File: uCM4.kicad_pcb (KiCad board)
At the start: 2 copper layers, 55 x 48 mm, 77 parts, among them IC1 MAX17048G+, J10 USB_C_Receptacle, J12 Conn_02x08_Odd_Even, J13 Conn_02x07_Odd_Even, J2 Micro_SD_Card_Det, J4 Conn_01x04, J5 DummyJ, J6 DummyJ, J8 Camera 0, J9 Camera 1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

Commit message: Routing
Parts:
- removed TP1, TP3, TP4, TP5, TP6, TP7, TP9: TestPoint, TestPoint:TestPoint_Pad_D1.0mm
- removed U3: TPD4EUSB30DQAR, Package_SON:USON-10_2.5x1.0mm_P0.5mm
- added U5: TPD2EUSB30, Package_TO_SOT_SMD:Texas_DRT-3, F.Cu at (150.0, 125.8)
- moved TP10 34.3 mm to (122.5, 125.0)
- moved TP11 32.6 mm to (122.5, 129.2)
- moved TP2 9.05 mm to (142.8, 105.2)
- moved TP8 8.63 mm to (133.8, 96.5)
- moved TP12 8.49 mm to (140.0, 107.8)
- moved S2 0.75 mm to (158.5, 108.8)
- moved S1 0.25 mm to (158.5, 99.5)
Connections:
- Module1 pad 37: /ENV_SEL -> unconnected-(Module1A-GPIO7-Pad37)
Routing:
- net GND: track 1.88 -> 137.5 mm, vias 29 -> 95
- net +3V3: track 14.8 -> 141.7 mm, vias 0 -> 19
- net /CAM_GPIO: track 0.00 -> 77.1 mm, vias 0 -> 9
- net /USB_P: track 11.8 -> 78.7 mm, vias 0 -> 1
- net /USB_N: track 13.0 -> 78.2 mm, vias 0 -> 1
- net +5V: track 32.8 -> 97.9 mm, vias 2 -> 8
- net /SCL0: track 40.2 -> 102.7 mm, vias 4 -> 5
- net /RESET: track 0.00 -> 62.0 mm, vias 0 -> 3
- net /SDA0: track 45.2 -> 107.0 mm, vias 4 -> 6
- net Net-(Module1A-Global_EN): track 3.85 -> 59.3 mm, vias 0 -> 3
- net /TXD0: track 0.00 -> 50.3 mm, vias 0 -> 5
- net Net-(Module1A-nRPIBOOT): track 0.00 -> 46.5 mm, vias 0 -> 5
- net /SPI6_CE1_N: track 0.00 -> 41.0 mm, vias 0 -> 5
- net /SCL1: track 3.60 -> 42.4 mm, vias 0 -> 5
- net /SPI6_CE0_N: track 0.00 -> 37.6 mm, vias 0 -> 3
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- added copper zone on F.Cu, net GND
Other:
- board text removed: "ACT"
- board text removed: "PWR"
- board text removed: "RESET"
- board text removed: "RPIBOOT"
- board text removed: "RX GND TX"
- board text removed: "USB OTG"

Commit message: Updating LCSC numbers.
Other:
- board text removed: "(C) Kamil Lorenc 2021"
- board text removed: "µCM4-Net v0.2.0"
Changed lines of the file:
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@@
 		(layer "User.2")
-	)
-	(gr_text "µCM4-Net v0.2.0"
-		(at 126.5 111.5 270)
-		(layer "B.SilkS")
-		(effects
-			(font
-				(size 1 1)
-				(thickness 0.15)
-			)
-			(justify mirror)
-		)
-	)
-	(gr_text "(C) Kamil Lorenc 2021"
-		(at 124.5 109.5 270)
-		(layer "B.SilkS")
-		(effects
-			(font
-				(size 1 1)
-				(thickness 0.15)
-			)
-			(justify mirror)
-		)
 	)
 	(gr_text "Check GPS orientation. And pinout needs to change."

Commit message: Minor changes
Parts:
- J2: footprint CM4:SDCARD_MOLEX_503398-1892 -> Connector_Card:microSD_HC_Hirose_DM3AT-SF-PEJM5

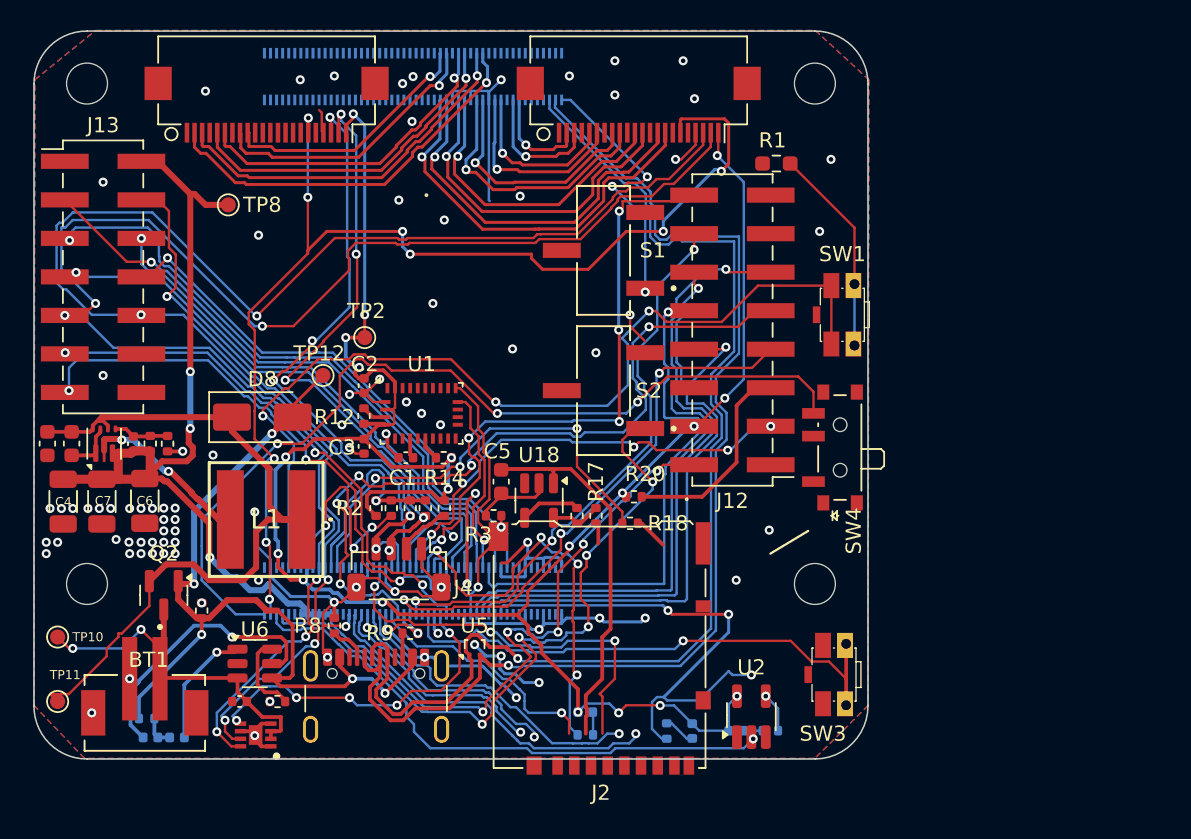
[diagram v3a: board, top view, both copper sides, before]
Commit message: Tuning differential traces and changing some footprints
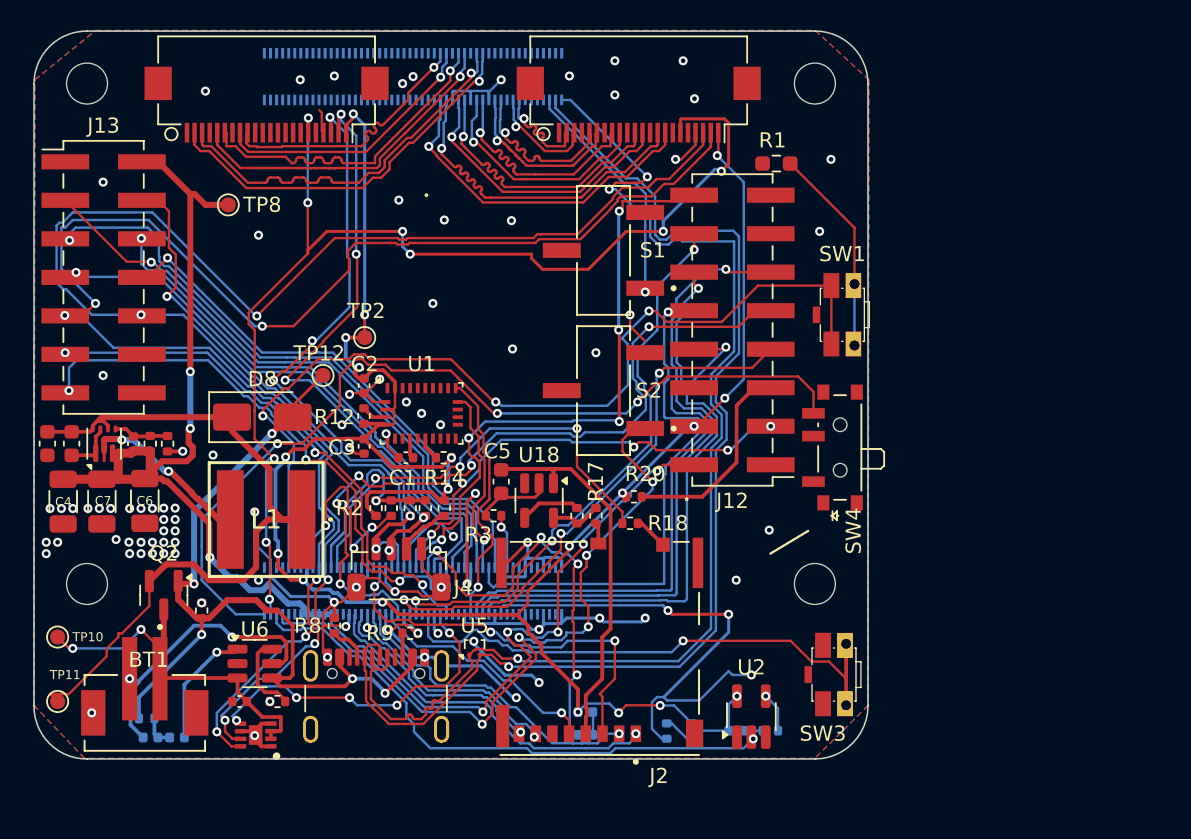
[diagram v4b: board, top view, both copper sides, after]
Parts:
- J2: footprint Connector_Card:microSD_HC_Hirose_DM3AT-SF-PEJM5 -> CM4:SDCARD_MOLEX_503398-1892
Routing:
- net GND: track 137.5 -> 130.3 mm, vias 95 -> 93
- net /CAM1_D3_P: track 26.6 -> 22.9 mm
- net /CAM1_D2_P: track 22.5 -> 19.0 mm
- net /CAM1_C_P: track 17.7 -> 15.4 mm
- net /CAM1_D3_N: track 24.9 -> 22.9 mm
- net /CAM1_D1_P: track 12.8 -> 11.4 mm
- net /CAM1_D2_N: track 20.3 -> 18.9 mm
- net /CAM1_D0_P: track 8.59 -> 7.29 mm
- net /CAM0_D0_P: track 24.5 -> 25.8 mm
- net /CAM0_C_P: track 17.1 -> 18.0 mm
- net /CAM0_C_N: track 18.7 -> 18.0 mm
- net /CAM0_D1_P: track 21.3 -> 22.0 mm
- net /CAM0_D1_N: track 22.6 -> 22.0 mm
- net /USB_P: track 78.7 -> 78.1 mm
- net /SD_CLK: track 16.3 -> 15.7 mm
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
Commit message: Prepping for production.
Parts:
- C5: value 10u -> 10uF
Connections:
- U6 pad 2: unconnected-(U6-GND-Pad2) -> GND
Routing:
- net GND: track 130.3 -> 131.7 mm, vias 93 -> 94
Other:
- board text added: "Shepherd's Eye V1.0 William Nacci Kemere/RNEL + Robinson Labs '25"

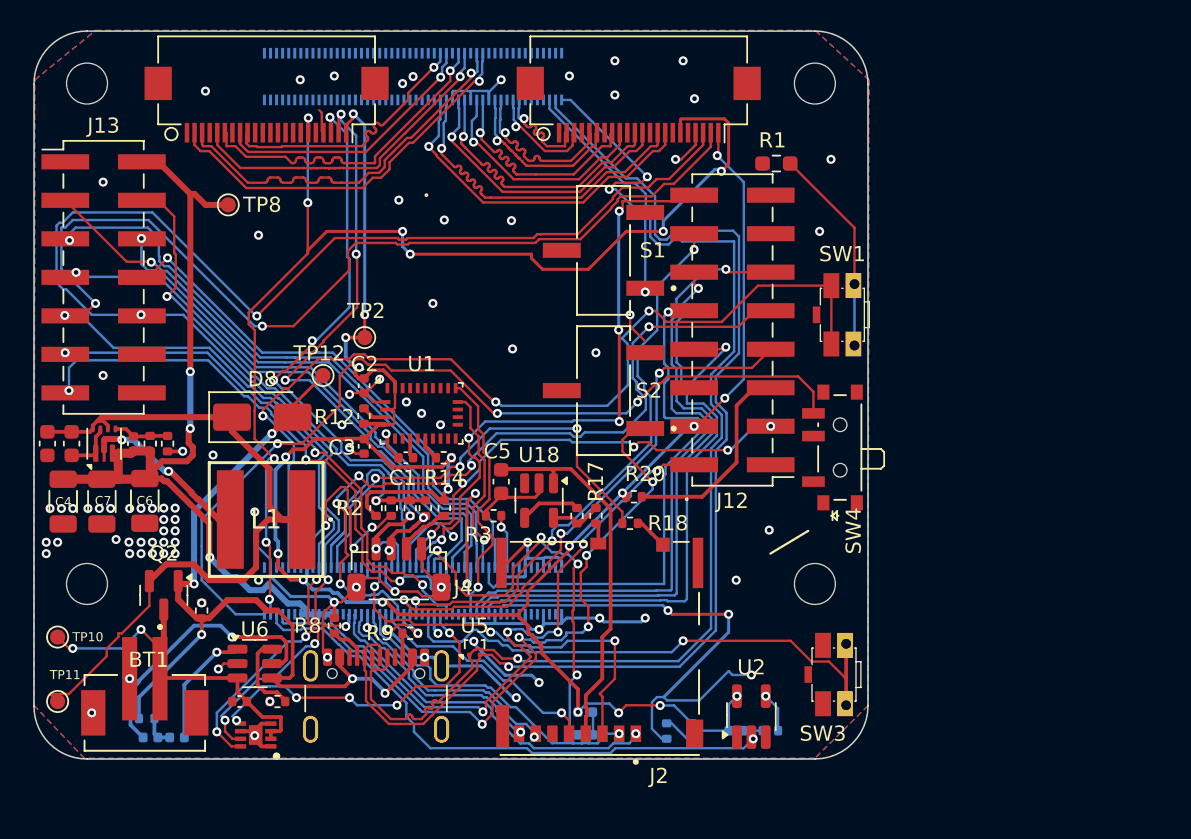
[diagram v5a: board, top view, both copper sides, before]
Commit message: Added new camera connectors. (Had to flip the symbol to match up hirose connection order)
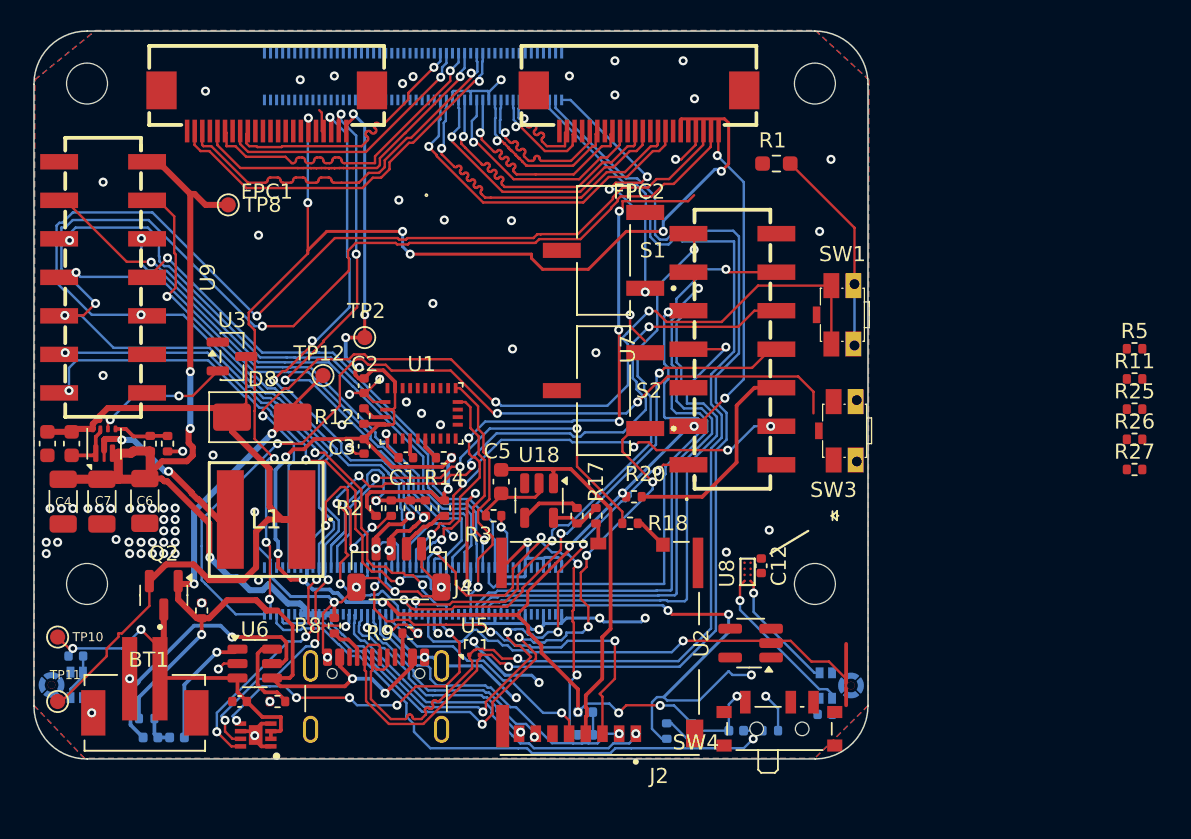
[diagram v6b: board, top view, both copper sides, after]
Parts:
- removed J12: Conn_02x08_Odd_Even, Connector_PinHeader_2.54mm:PinHeader_2x08_P2.54mm_Vertical_SMD
- removed J13: Conn_02x07_Odd_Even, Connector_PinHeader_2.54mm:PinHeader_2x07_P2.54mm_Vertical_SMD
- removed J8: Camera 0, CM4:Hirose_FH12-22S-0.5SH_1x22-1MP_P0.50mm_Horizontal
- removed J9: Camera 1, CM4:Hirose_FH12-22S-0.5SH_1x22-1MP_P0.50mm_Horizontal
- added C10: 100nF, Capacitor_SMD:C_0402_1005Metric, B.Cu at (173.1, 130.1)
- added C12: 100nF, Capacitor_SMD:C_0402_1005Metric, F.Cu at (168.9, 120.3)
- added FPC1: FPC-05F-22PH20, EasyEDA:FPC-SMD_22P-P0.50_FPC-05F-22PH20, F.Cu at (136.3, 90.3)
- added FPC2: FPC-05F-22PH20, EasyEDA:FPC-SMD_22P-P0.50_FPC-05F-22PH20, F.Cu at (160.8, 90.3)
- added MIC1: MMICT390200012, EasyEDA:MIC-SMD_5P-L3.5-W2.7-TL_MMICT390200012, B.Cu at (174.1, 128.2)
- added MIC2: MMICT390200012, EasyEDA:MIC-SMD_5P-L3.5-W2.7-TL_MMICT390200012, B.Cu at (122.8, 128.2)
- added R11: 2.2K 1%, Resistor_SMD:R_0402_1005Metric, F.Cu at (193.5, 108.0)
- added R25: 2.2K 1%, Resistor_SMD:R_0402_1005Metric, F.Cu at (193.5, 110.0)
- added R26: 2.2K 1%, Resistor_SMD:R_0402_1005Metric, F.Cu at (193.5, 112.0)
- added R27: 1k, Resistor_SMD:R_0402_1005Metric, F.Cu at (193.5, 114.0)
- added R5: 2.2K 1%, Resistor_SMD:R_0402_1005Metric, F.Cu at (193.5, 106.0)
- added U3: TPS3839DBZ, Package_TO_SOT_SMD:SOT-23, F.Cu at (134.0, 106.5)
- added U7: HC-PM254-5.0H-2X7PS, EasyEDA:HDR-SMD_14P-P2.54-V-F-R2-C7-LS7.4, F.Cu at (167.0, 106.0)
- added U8: ADAU7002ACBZ-R7, EasyEDA:WLCSP-8_L1.6-W0.8-R2-C4-P0.40-TL, F.Cu at (168.0, 120.7)
- added U9: HC-PM254-5.0H-2X7PS, EasyEDA:HDR-SMD_14P-P2.54-V-F-R2-C7-LS7.4, F.Cu at (125.5, 101.3)
- C11: value 105pF -> 100nF; moved to B.Cu
- Q2: value AO3401A -> SI2369DS
- R19: value 760k -> 750k
- moved SW4 18.6 mm to (170.1, 130.7), turned to 0 degrees
- moved SW3 16.1 mm to (174.4, 111.4)
- moved C11 14.5 mm to (123.7, 126.3), turned to 180 degrees
- moved U2 4.85 mm to (168.2, 125.4), turned to 180 degrees
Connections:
- C11 pad 1: +5V -> +3V3
- C11 pad 2: Net-(U4-FB) -> GND
- D7 pad 2: Net-(D6-A) -> Net-(D7-A)
- IC1 pad 7: /SCL0 -> /SCL3
- IC1 pad 8: /SDA0 -> /SDA3
- J4 pad 3: /SDA1 -> /SCL3
- J4 pad 4: /SCL1 -> /SDA3
- Module1 pad 25: /SPI6_SCLK -> unconnected-(Module1A-GPIO21-Pad25)
- Module1 pad 26: /SPI6_MISO -> /PCM_FS
- Module1 pad 27: /SPI6_MOSI -> /PCM_DIN
- Module1 pad 35: unconnected-(Module1A-ID_SC-Pad35) -> GND
- Module1 pad 36: unconnected-(Module1A-ID_SD-Pad36) -> /SDA1
- Module1 pad 37: unconnected-(Module1A-GPIO7-Pad37) -> /GPIO7
- Module1 pad 46: /GPIO22 -> /SDA6
- Module1 pad 47: unconnected-(Module1A-GPIO23-Pad47) -> /SCL6
- Module1 pad 48: /SPI6_CE1_N -> unconnected-(Module1A-GPIO27-Pad48)
- Module1 pad 49: /SPI6_CE0_N -> /PCM_CLK
- Module1 pad 56: /SCL1 -> /SCL3
- Module1 pad 58: /SDA1 -> /SDA3
- R10 pad 1: /GPIO22 -> /GPIO7
- R17 pad 1: /+3.3v -> +3V3
- R24 pad 2: Net-(D6-A) -> Net-(D7-A)
- R29 pad 1: /+3.3v -> +3V3
- R7 pad 1: /SCL1 -> GND
- S1 pad 1: Net-(Module1B-USB_OTG_ID) -> unconnected-(S1-Pad1)
- S1 pad 2: unconnected-(S1-Pad2) -> Net-(Module1B-USB_OTG_ID)
- S2 pad 1: Net-(Module1A-nRPIBOOT) -> unconnected-(S2-Pad1)
- S2 pad 2: unconnected-(S2-Pad2) -> Net-(Module1A-nRPIBOOT)
- U1 pad 19: /RXD5 -> /TXD5
- U1 pad 20: /TXD5 -> /RXD5
- U18 pad 5: /+3.3v -> +3V3
- U4 pad 5: /BOOST_IN -> Net-(U3-~{RESET})
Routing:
- net (no net): track 0.00 -> 70.2 mm, vias 0 -> 4
- net /SCL1: track 42.4 -> 0.00 mm, vias 5 -> 0
- net unconnected-(Module1A-GPIO27-Pad48): track 0.00 -> 41.0 mm, vias 0 -> 5
- net /SPI6_CE1_N: track 41.0 -> 0.00 mm, vias 5 -> 0
- net /SPI6_MOSI: track 38.5 -> 0.00 mm, vias 1 -> 0
- net /PCM_DIN: track 0.00 -> 38.5 mm, vias 0 -> 1
- net /SPI6_CE0_N: track 37.6 -> 0.00 mm, vias 3 -> 0
- net /PCM_CLK: track 0.00 -> 37.6 mm, vias 0 -> 3
- net /SPI6_MISO: track 36.2 -> 0.00 mm, vias 1 -> 0
- net /PCM_FS: track 0.00 -> 36.2 mm, vias 0 -> 1
- net unconnected-(Module1A-GPIO21-Pad25): track 0.00 -> 36.0 mm, vias 0 -> 1
- net /SPI6_SCLK: track 36.0 -> 0.00 mm, vias 1 -> 0
- net /GPIO22: track 27.8 -> 0.00 mm, vias 4 -> 0
- net /PDM_CLK: track 0.00 -> 10.7 mm, vias 0 -> 1
- net Net-(U3-~{RESET}): track 0.00 -> 9.10 mm, vias 0 -> 2
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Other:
- board text added: "EweGo V1.0 William Nacci Kemere/RNEL + Robinson Labs '25"
- board text removed: "Shepherd's Eye V1.0 William Nacci Kemere/RNEL + Robinson Labs '25"

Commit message: Routing in progress
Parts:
- removed TP10: TestPoint, TestPoint:TestPoint_Pad_D1.0mm
- R27: moved to B.Cu
- moved R27 66.7 mm to (128.8, 130.2), turned to -90 degrees
- moved R11 50.9 mm to (143.4, 116.9), turned to 90 degrees
- moved R5 50.2 mm to (144.5, 116.9), turned to 90 degrees
- moved R26 47.3 mm to (146.4, 116.9), turned to 90 degrees
- moved R25 46.6 mm to (147.4, 116.9), turned to 90 degrees
- moved SW3 43.8 mm to (135.1, 130.7), turned to 0 degrees
- moved TP11 25.8 mm to (141.0, 111.2)
- moved C13 24.7 mm to (146.7, 107.7)
- moved IC1 24.7 mm to (147.8, 110.0)
- moved R7 14.7 mm to (154.4, 104.7), turned to 135 degrees
- moved R10 13.9 mm to (143.5, 130.0)
- moved D3 13.8 mm to (143.5, 131.0)
- moved R6 13.0 mm to (153.6, 105.5), turned to 135 degrees
- moved SW1 11.4 mm to (174.2, 115.1)
- moved R4 9.33 mm to (137.8, 123.0), turned to -90 degrees
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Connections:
- FPC2 pad 3: GND -> /SCL1
- Module1 pad 35: GND -> /SCL1
- R23 pad 1: +3V3 -> /GPIO_VREF
- R25 pad 2: Net-(R25-Pad2) -> /GPIO_VREF
- R26 pad 2: Net-(R25-Pad2) -> /GPIO_VREF
- R7 pad 1: GND -> /SCL1
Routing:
- net /SDA0: track 107.0 -> 0.00 mm, vias 6 -> 0
- net /SCL0: track 102.7 -> 0.00 mm, vias 5 -> 0
- net (no net): track 70.2 -> 0.00 mm, vias 4 -> 0
- net /PDM_CLK: track 10.7 -> 70.1 mm, vias 1 -> 3
- net /PDM_DAT: track 8.14 -> 63.4 mm, vias 1 -> 3
- net /SCL1: track 0.00 -> 47.2 mm, vias 0 -> 3
- net unconnected-(Module1A-GPIO27-Pad48): track 41.0 -> 0.00 mm, vias 5 -> 0
- net unconnected-(Module1A-GPIO21-Pad25): track 36.0 -> 0.00 mm, vias 1 -> 0
- net /BTN0: track 35.5 -> 0.00 mm, vias 1 -> 0
- net /SDA3: track 0.00 -> 35.1 mm, vias 0 -> 4
- net GND: track 131.7 -> 99.8 mm, vias 99 -> 85
- net /SCL3: track 0.00 -> 31.6 mm, vias 0 -> 4
- net +3V3: track 148.2 -> 170.5 mm
- net /BAT_ALERT: track 22.3 -> 0.00 mm, vias 5 -> 0
- net Net-(Module1A-Global_EN): track 59.3 -> 81.5 mm, vias 3 -> 5
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
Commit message: Routed and should be ready to order
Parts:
- removed SW3: SW_Push, KiCAD_Randoms:PTS840_PM_SMTR_LFS
- removed SW4: SW_SPDT, Button_Switch_SMD:SW_SPDT_PCM12
- added B1: SW_DIP_x01, KiCAD_Randoms:PTS840_PM_SMTR_LFS, F.Cu at (174.2, 115.0)
- added B2: SW_Push, KiCAD_Randoms:PTS840_PM_SMTR_LFS, F.Cu at (135.1, 130.7)
- added TP1: TestPoint, TestPoint:TestPoint_Pad_D1.0mm, F.Cu at (174.8, 92.4)
- S3: renamed from SW1; value SW_DIP_x01 -> SW_SPDT; footprint KiCAD_Randoms:PTS840_PM_SMTR_LFS -> Button_Switch_SMD:SW_SPDT_PCM12
- U2: moved to B.Cu
- moved D1 32.8 mm to (134.4, 130.0)
- moved R13 32.8 mm to (136.7, 130.0)
- moved U2 32.4 mm to (135.9, 127.4), turned to 0 degrees
- moved R1 21.4 mm to (171.2, 115.2), turned to 90 degrees
- moved S3 15.9 mm to (170.1, 130.4), turned to 0 degrees
- moved TP11 11.8 mm to (139.8, 99.5)
- moved R20 10.9 mm to (171.0, 112.8)
- moved C13 1.85 mm to (148.5, 108.1)
- moved D3 1.50 mm to (142.0, 131.0)
- moved R10 1.50 mm to (142.0, 130.0)
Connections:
- R1 pad 1: Net-(R1-Pad1) -> Net-(B1-Pad1)
- S3 pad 1: Net-(R1-Pad1) -> unconnected-(S3-A-Pad1)
- S3 pad 2: /RESET -> GND
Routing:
- net /BAT: track 11.8 -> 98.7 mm, vias 0 -> 5
- net /BAT_ALERT: track 0.00 -> 59.2 mm, vias 0 -> 3
- net +3V3: track 170.5 -> 225.8 mm, vias 19 -> 18
- net /BOOST_IN: track 41.2 -> 85.7 mm, vias 1 -> 2
- net VBUS: track 56.0 -> 94.8 mm, vias 5 -> 7
- net /nPWR_LED: track 42.7 -> 5.24 mm, vias 1 -> 0
- net /SDA0: track 0.00 -> 36.6 mm, vias 0 -> 3
- net /SCL0: track 0.00 -> 35.9 mm, vias 0 -> 3
- net /SDA6: track 5.68 -> 40.4 mm, vias 1 -> 2
- net /SCL6: track 6.48 -> 34.2 mm, vias 1 -> 3
- net GND: track 99.8 -> 125.0 mm, vias 85 -> 127
- net /BTN0: track 0.00 -> 23.3 mm, vias 0 -> 2
- net +5V: track 97.8 -> 119.0 mm, vias 8 -> 10
- net /GPIO7: track 0.00 -> 18.9 mm, vias 0 -> 2
- net Net-(R1-Pad1): track 17.8 -> 0.00 mm
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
